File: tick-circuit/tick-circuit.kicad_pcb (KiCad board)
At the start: 2 copper layers, 45.7 x 33 mm, 14 parts, among them J1 Power, J2 50/60Hz, U1 74HCT4060, U2 74HCT73, X1 3.93216 MHz

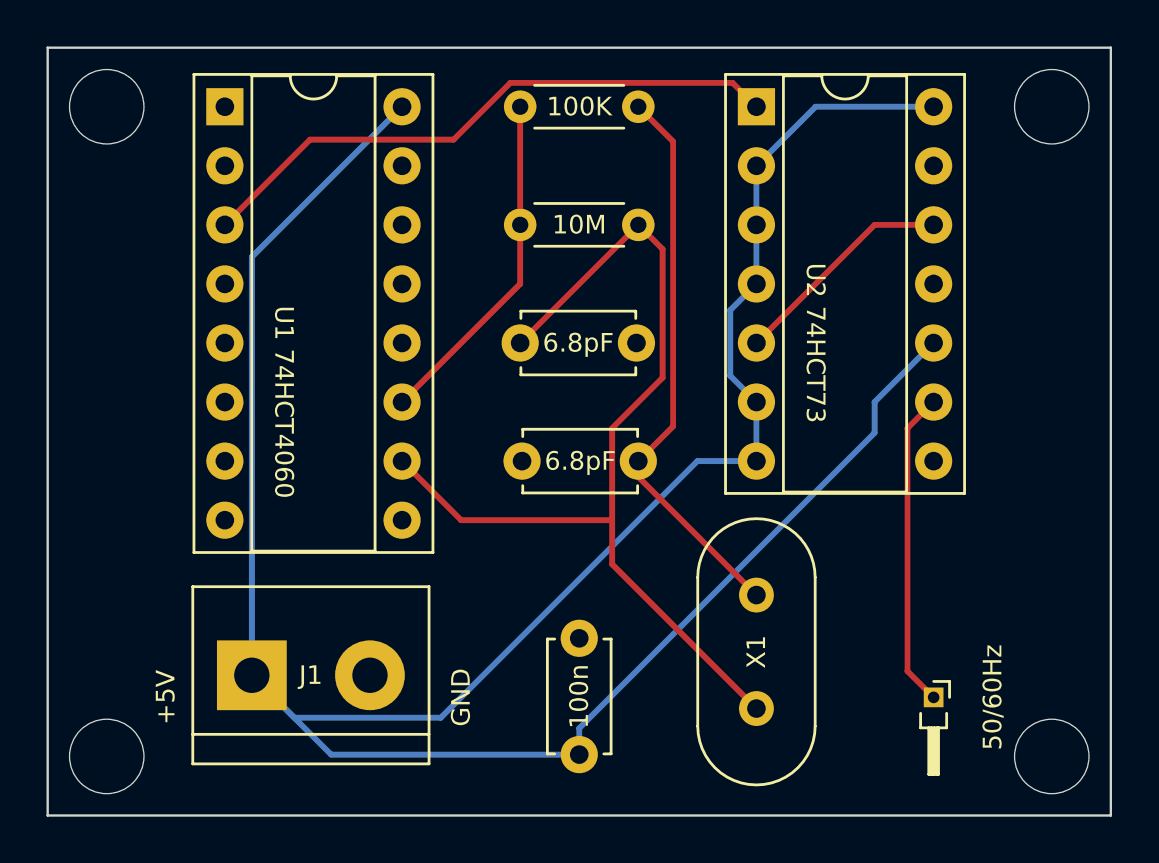
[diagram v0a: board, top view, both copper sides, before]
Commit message: Change resistor footprints, change J2 footprint, alter routing to match, move 5v away from gnd, add URL to pcb
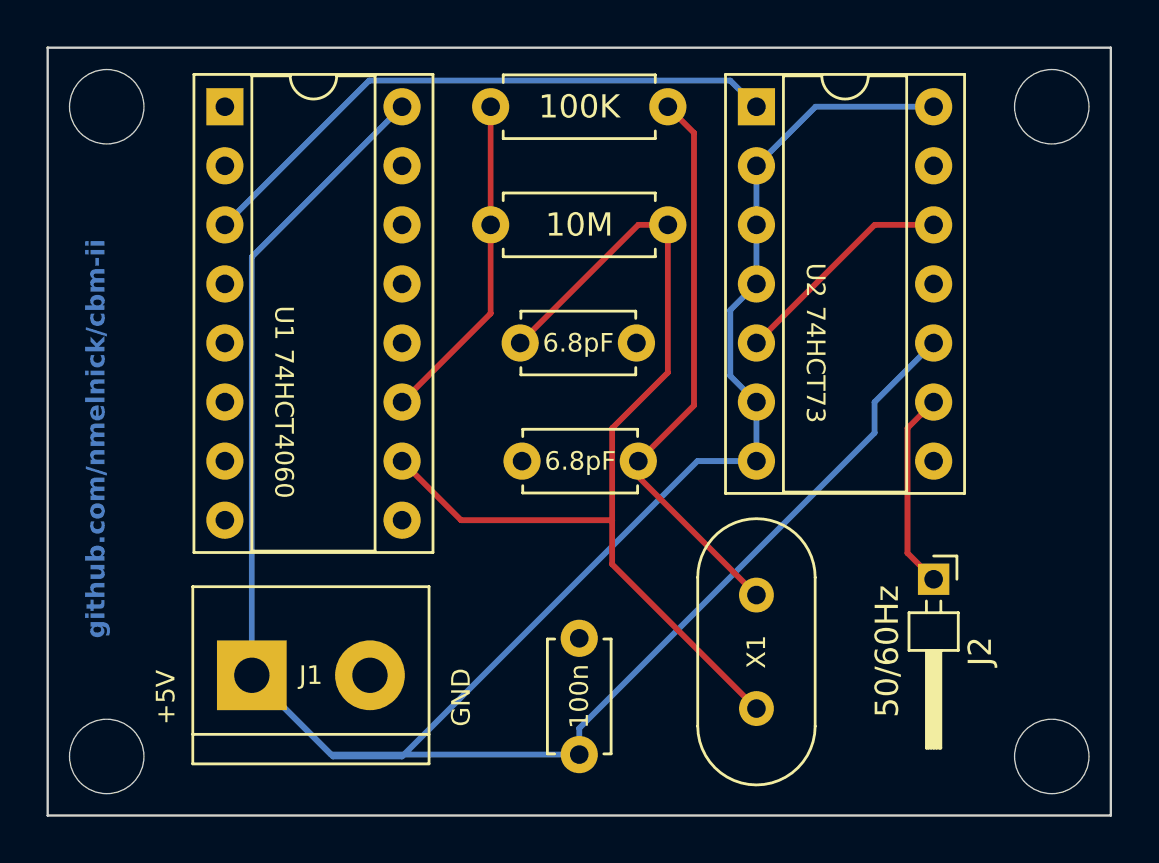
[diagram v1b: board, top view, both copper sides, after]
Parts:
- J2: footprint Connector_PinHeader_1.00mm:PinHeader_1x01_P1.00mm_Horizontal -> Connector_PinHeader_2.00mm:PinHeader_1x01_P2.00mm_Horizontal
- R1, R2: footprint Resistor_THT:R_Axial_DIN0204_L3.6mm_D1.6mm_P5.08mm_Horizontal -> Resistor_THT:R_Axial_DIN0207_L6.3mm_D2.5mm_P7.62mm_Horizontal
- moved J2 5.08 mm to (50.8, 35.6)
- moved R2 1.27 mm to (31.8, 15.2)
- moved R1 1.27 mm to (39.4, 20.3)
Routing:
- net Net-(J2-Pin_1): track 13.6 -> 8.55 mm
- net +5V: track 116.0 -> 117.3 mm
- net Net-(U1-RTC): track 42.5 -> 43.4 mm
- net Net-(U1-RS): track 14.8 -> 14.1 mm
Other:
- board text added: "github.com/nmelnick/cbm-ii"
